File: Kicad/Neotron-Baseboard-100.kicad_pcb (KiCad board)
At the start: 4 copper layers, 243.8 x 170.2 mm, 252 parts, among them J1001 USB Ports External, J1002 USB Ports Internal, J101 Neotron-Expansion-Slot, J102 Neotron-Expansion-Slot, J103 Neotron-Expansion-Slot, J104 Neotron-Expansion-Slot, J1101 RJ45 MagJack, J201 DE15HD, J601 Line Out, J602 AC'97 Audio Header, J603 CD Audio In, J701 SD_Card, J801 Conn_02x05, J802 DB9_Male_MountingHoles, J901 Jack-DC, J902 Conn_01x04, J903 Double-mini-DIN-6, SW901 SW_DIP_x01, SW902 SW_DIP_x01, U1001 AP2501, U1002 MIC2005A-2YM5, U1003 MIC2005A-2YM5, U1004 XR22404CG28, U1005 MIC2005A-2YM5, U1006 MIC2005A-2YM5, U101 Neotron-CPU, U1101 ENC424J600, U1201 MCP7940, U201 THS7316, U202 TPD7S019, U601 TLV320AIC23BPW, U602 STX-4335-5BGP-S1, U801 ST3232CDR, U901 5V DC-DC Module, U902 3v3 LDO, U903 MAX1615, U904 MKE04P24M48SF0, Y1001 12M, Y1101 25M, Y1201 32,768 Hz, Y601 12M

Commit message: Updating to common 0.5.0
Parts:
- removed the J902 at (226.9, 52.6)
- removed the R903 at (223.9, 58.2)
- added C909: 100n, Capacitor_SMD:C_0805_2012Metric_Pad1.15x1.40mm_HandSolder, F.Cu at (241.5, 98.0)
- added JP901: Jumper, Connector_PinHeader_2.54mm:PinHeader_1x02_P2.54mm_Vertical, F.Cu at (239.0, 105.7)
- added JP902: Jumper, Connector_PinHeader_2.54mm:PinHeader_1x02_P2.54mm_Vertical, F.Cu at (246.4, 105.7)
- added JP903: Jumper, Connector_PinHeader_2.54mm:PinHeader_1x02_P2.54mm_Vertical, F.Cu at (243.8, 105.7)
- added Q901: BC548, Package_TO_SOT_THT:TO-92_HandSolder, F.Cu at (246.8, 93.0)
- added R904: 10k, Resistor_SMD:R_0805_2012Metric_Pad1.15x1.40mm_HandSolder, F.Cu at (256.2, 97.8)
- added R909: 10k, Resistor_SMD:R_0805_2012Metric_Pad1.15x1.40mm_HandSolder, F.Cu at (256.2, 107.8)
- added TP902: TestPoint, Connector_PinHeader_2.54mm:PinHeader_1x01_P2.54mm_Vertical, F.Cu at (236.4, 108.3)
- added TP903: TestPoint, Connector_PinHeader_2.54mm:PinHeader_1x01_P2.54mm_Vertical, F.Cu at (241.5, 108.3)
- C901, C902: footprint Capacitor_THT:CP_Radial_D8.0mm_P3.50mm -> Capacitor_THT:CP_Radial_D6.3mm_P2.50mm
- C905: value 47u -> 1u; footprint Capacitor_THT:CP_Radial_D6.3mm_P2.50mm -> Capacitor_SMD:C_0805_2012Metric_Pad1.15x1.40mm_HandSolder
- F901: value 6A PTC -> 32V 2A PTC; footprint Fuse:Fuse_Bourns_MF-RG500 -> Fuse:Fuse_BelFuse_0ZRE0016FF_L9.9mm_W3.8mm
- L901: value 22u -> 22uH 6A; footprint Inductor_THT:L_Axial_L23.4mm_D12.7mm_P7.62mm_Vertical_Vishay_IHA-203 -> Inductor_THT:L_Axial_L26.0mm_D11.0mm_P7.62mm_Vertical_Fastron_77A
- R901: value 100k -> 2k
- R902, R905, R907, R908: value 100k -> 10k
- R906: value 33k -> 10k
- TP901: value Reset -> TestPoint; footprint TestPoint:TestPoint_THTPad_2.0x2.0mm_Drill1.0mm -> Connector_PinHeader_2.54mm:PinHeader_1x01_P2.54mm_Vertical
- U902: value 3v3 LDO -> TLV1117 3.3V 1A; footprint Package_TO_SOT_SMD:TO-252-3_TabPin2 -> Package_TO_SOT_SMD:SOT-223-3_TabPin2
- U904: value MKE04P24M48SF0 -> STM32F030F4Px; footprint Package_SO:SOIC-20W_7.5x12.8mm_P1.27mm -> Package_SO:TSSOP-20_4.4x6.5mm_P0.65mm
- Y1201: footprint Crystal:Crystal_C26-LF_D2.1mm_L6.5mm_Horizontal -> Crystal:Crystal_DS26_D2.0mm_L6.0mm_Horizontal
- moved TP901 291.5 mm to (239.0, 108.3), turned to 180 degrees
- moved SW901 61.6 mm to (255.2, 114.9)
- moved SW902 61.6 mm to (255.2, 110.9)
- moved R902 51.1 mm to (256.2, 93.8), turned to 0 degrees
- moved D901 46.4 mm to (258.0, 119.2)
- moved R907 42.1 mm to (256.2, 103.8)
- moved C908 40.3 mm to (251.5, 98.0), turned to 90 degrees
- moved R903 38.8 mm to (256.2, 95.8), turned to 0 degrees
- moved R905 36.7 mm to (256.2, 99.8)
- moved R908 35.7 mm to (256.2, 105.8), turned to 180 degrees
- moved R906 33.8 mm to (256.2, 101.8), turned to 0 degrees
- moved U904 33.8 mm to (246.5, 100.0)
- moved U902 29.0 mm to (257.8, 74.3), turned to 90 degrees
- moved R901 27.5 mm to (256.2, 91.8), turned to 180 degrees
- moved C905 25.2 mm to (256.3, 80.0)
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- renumbered J903 to J902, R904 to R903
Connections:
- C907 pad 1: +5VP -> +3.3VP
- C908 pad 1: +5VP -> +3.3VP
- R901 pad 1: /Power Supply/DC_ON -> Net-(Q901-Pad2)
- R901 pad 2: GND -> /Power Supply/DC_ON
- R902 pad 1: +5VP -> /Power Supply/DC_ON
- R902 pad 2: /Power Supply/SWDCLK -> GND
- R903 pad 1: /Power Supply/STATUS_LED -> /Power Supply/~STATUS_LED
- R905 pad 2: /Power Supply/MON_5V -> Net-(R905-Pad2)
- R907 pad 1: /Power Supply/MON_5V -> Net-(R905-Pad2)
- R907 pad 2: GND -> /Power Supply/MON_5V
- RN901 pad 4: /Power Supply/PS2_DAT1 -> /Power Supply/PS2_CLK1
- RN901 pad 5: /Power Supply/PS2_CLK1 -> /Power Supply/PS2_DAT1
- SW901 pad 2: /Power Supply/~RESET_SW -> /Power Supply/~BUTTON_RST
- SW902 pad 2: /Power Supply/~POWER_SW -> /Power Supply/~BUTTON_PWR
- TP901 pad 1: Net-(TP901-Pad1) -> /Power Supply/USART1_TX
- U101 pad 4.3: /SD Card/DAT2 -> /SD Card/DAT1
- U101 pad 4.4: /SD Card/DAT3 -> /SD Card/DAT0
- U101 pad 4.5: /SD Card/CMD -> /SD Card/CLK
- U101 pad 4.6: /SD Card/CLK -> /SD Card/CMD
- U101 pad 4.7: /SD Card/DAT0 -> /SD Card/DAT3
- U101 pad 4.8: /SD Card/DAT1 -> /SD Card/DAT2
- U901 pad 1: /Power Supply/DC_ON -> /Power Supply/~PSU_EN
- U903 pad 3: +5VP -> +3.3VP
- U903 pad 4: +5VP -> GND
- U904 pad 1: Net-(TP901-Pad1) -> /Power Supply/BOOT0
- U904 pad 10: /Power Supply/PS2_CLK1 -> /Power Supply/DC_ON
- U904 pad 11: /Power Supply/PS2_DAT0 -> /~RESET
- U904 pad 12: /Power Supply/PS2_CLK0 -> /Power Supply/~BUTTON_RST
- U904 pad 13: /Power Supply/~RESET_SW -> /Power Supply/~BUTTON_PWR
- U904 pad 15: /Power Supply/UART0_TX -> GND
- U904 pad 16: /Power Supply/MON_3V3 -> +3.3VP
- U904 pad 17: /I2C_SCL -> /Power Supply/SCL_U1TX
- U904 pad 18: /I2C_SDA -> /Power Supply/SDA_U1RX
- U904 pad 19: /Power Supply/MON_5V -> /Power Supply/PS2_DAT1
- U904 pad 2: /Power Supply/SWDIO -> /Power Supply/PS2_DAT0
- U904 pad 20: /Power Supply/SWDCLK -> /Power Supply/PS2_CLK1
- U904 pad 3: +5VP -> /Power Supply/PS2_CLK0
- U904 pad 4: GND -> /Power Supply/~BMC_RST
- U904 pad 5: /Power Supply/STATUS_LED -> +3.3VP
- U904 pad 6: /Power Supply/DC_ON -> /Power Supply/MON_3V3
- U904 pad 7: /~RESET -> /Power Supply/MON_5V
- U904 pad 8: /Power Supply/~POWER_SW -> /Power Supply/USART1_TX
- U904 pad 9: /Power Supply/PS2_DAT1 -> /Power Supply/~STATUS_LED
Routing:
- net +5V: track 716.5 -> 130.8 mm, vias 9 -> 2
- net /~CS0: track 356.5 -> 0.00 mm, vias 1 -> 0
- net /~IRQ0: track 353.0 -> 0.00 mm, vias 1 -> 0
- net /I2C_SCL: track 337.1 -> 0.00 mm, vias 2 -> 0
- net /I2C_SDA: track 332.6 -> 0.00 mm, vias 2 -> 0
- net /~CS1: track 327.9 -> 0.00 mm, vias 1 -> 0
- net /~IRQ1: track 325.6 -> 0.00 mm, vias 1 -> 0
- net /~IRQ2: track 282.7 -> 0.00 mm
- net /~CS2: track 278.2 -> 0.00 mm
- net /~CS3: track 259.5 -> 0.00 mm
- net /~IRQ3: track 259.4 -> 0.00 mm
- net /~RESET: track 248.8 -> 0.00 mm, vias 2 -> 0
- net /SPI_CLK: track 215.1 -> 0.00 mm, vias 1 -> 0
- net /SPI_COPI: track 214.9 -> 0.00 mm, vias 1 -> 0
- net /SPI_CIPO: track 213.1 -> 0.00 mm, vias 1 -> 0
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
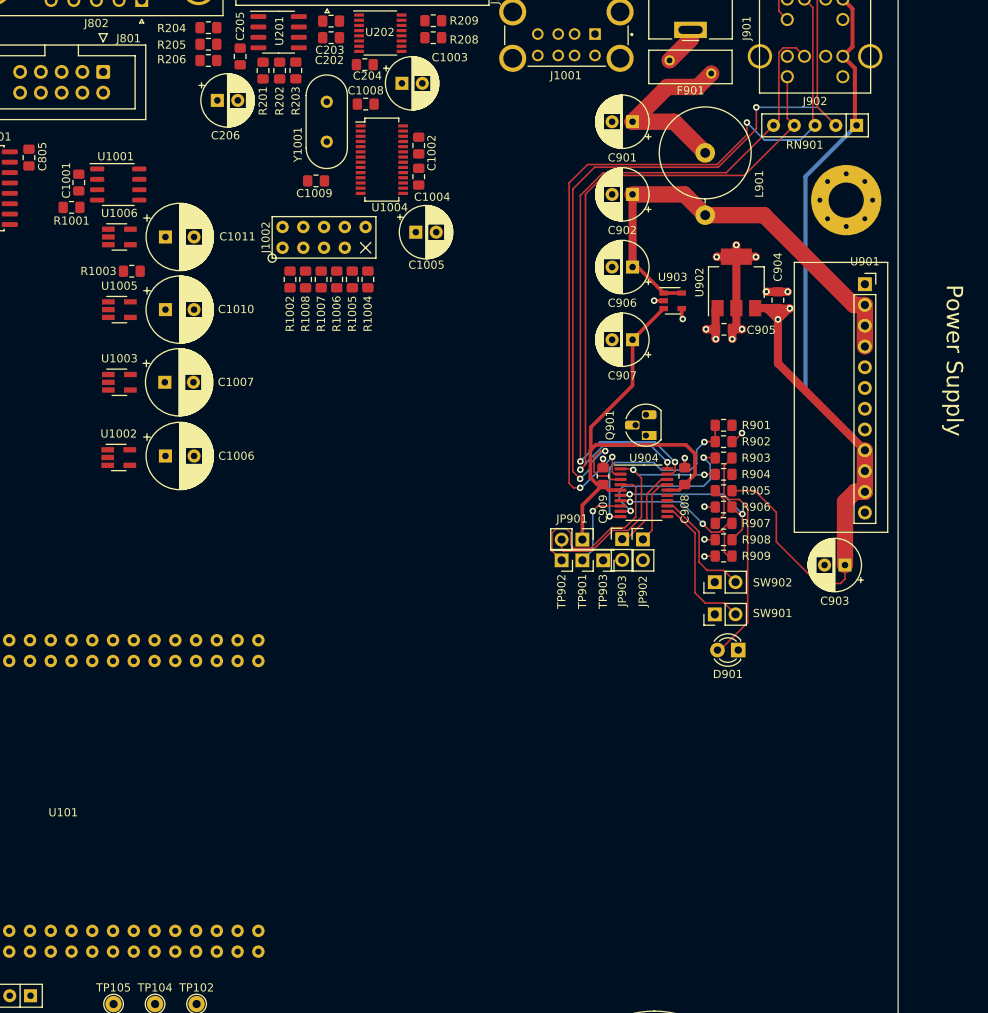
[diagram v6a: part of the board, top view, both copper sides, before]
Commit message: Updated to v0.6.0
Started re-laying out PSU
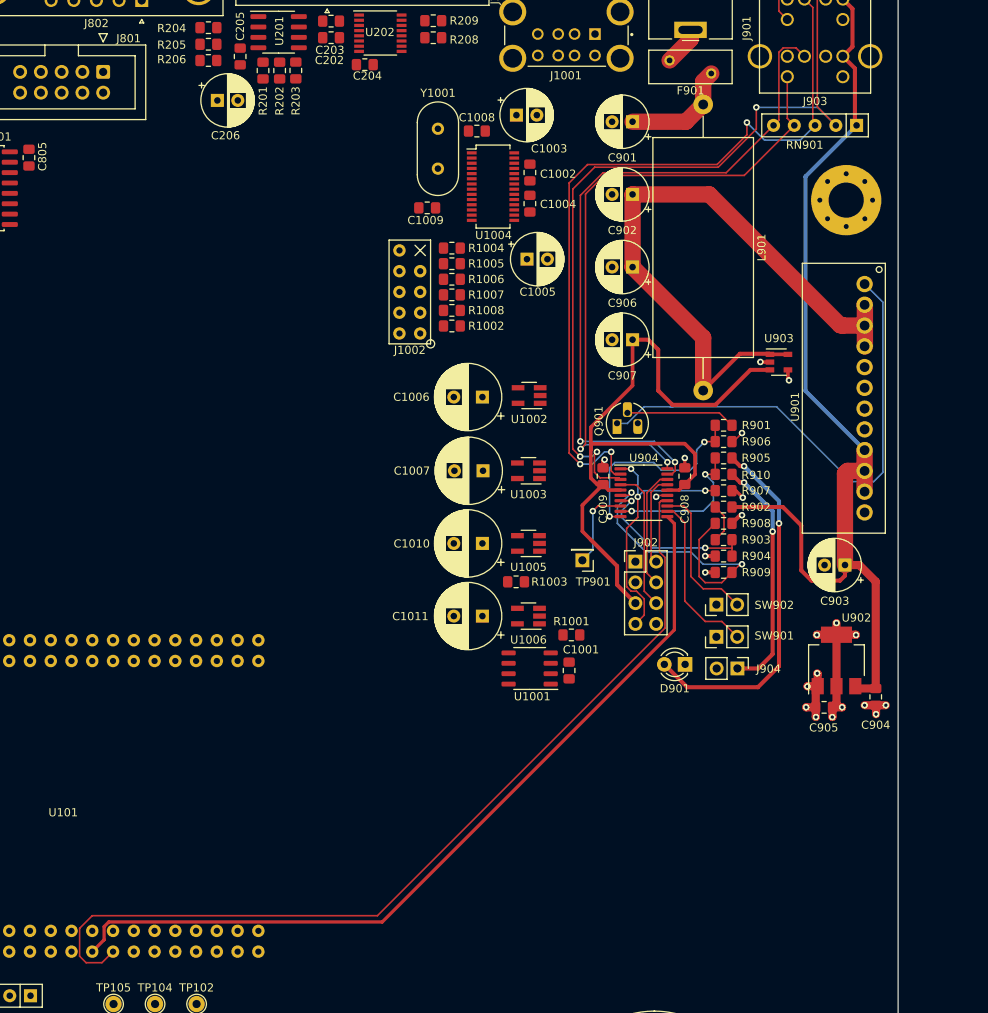
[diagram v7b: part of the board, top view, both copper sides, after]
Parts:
- removed JP901, JP902, JP903: Jumper, Connector_PinHeader_2.54mm:PinHeader_1x02_P2.54mm_Vertical
- removed the R909 at (256.2, 107.8)
- removed TP902, TP903: TestPoint, Connector_PinHeader_2.54mm:PinHeader_1x01_P2.54mm_Vertical
- added J902: Conn_02x04_Odd_Even, Connector_PinHeader_2.54mm:PinHeader_2x04_P2.54mm_Vertical, F.Cu at (245.5, 108.4)
- added J904: Header, Connector_PinHeader_2.54mm:PinHeader_1x02_P2.54mm_Vertical, F.Cu at (257.9, 121.5)
- added R904: 10k, Resistor_SMD:R_0805_2012Metric_Pad1.15x1.40mm_HandSolder, F.Cu at (256.2, 107.8)
- added R910: 1k, Resistor_SMD:R_0805_2012Metric_Pad1.15x1.40mm_HandSolder, F.Cu at (256.2, 97.8)
- L901: footprint Inductor_THT:L_Axial_L26.0mm_D11.0mm_P7.62mm_Vertical_Fastron_77A -> Inductor_THT:L_Axial_L26.7mm_D12.1mm_P35.00mm_Horizontal_Vishay_IHA-103
- U901: footprint Connector_PinSocket_2.54mm:PinSocket_1x12_P2.54mm_Vertical -> Neotron-Common-Hardware:K78xx-3AR3
- moved C1001 84.6 mm to (237.3, 121.8), turned to 270 degrees
- moved R1001 80.5 mm to (237.6, 117.4), turned to 180 degrees
- moved U1001 77.7 mm to (232.5, 121.5), turned to 180 degrees
- moved U1006 68.2 mm to (232.4, 115.1), turned to 180 degrees
- moved C1011 60.5 mm to (226.7, 115.1), turned to 180 degrees
- moved R1003 60.5 mm to (230.9, 110.9), turned to 0 degrees
- moved U1005 57.6 mm to (232.4, 106.2), turned to 180 degrees
- moved U1003 51.2 mm to (232.4, 97.3), turned to 180 degrees
- moved U1002 50.8 mm to (232.5, 88.1), turned to 180 degrees
- moved C904 50.0 mm to (274.9, 125.0), turned to 270 degrees
- moved C1010 48.2 mm to (226.7, 106.2), turned to 180 degrees
- moved C905 47.8 mm to (268.5, 126.3)
- moved U902 47.8 mm to (270.1, 120.5)
- moved C1007 40.4 mm to (226.8, 97.3), turned to 180 degrees
- moved C1006 39.4 mm to (226.7, 88.3), turned to 180 degrees
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- renumbered J902 to J903, R905 to R902, R907 to R903, R903 to R905, R902 to R906, R904 to R907, R906 to R908, R908 to R909
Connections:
- U901 pad 3: Net-(C902-Pad1) -> GND
- U901 pad 4: Net-(C902-Pad1) -> +5V
- U901 pad 5: GND -> (no net)
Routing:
- net /~IRQ7: track 0.59 -> 112.5 mm
- net /~RESET: track 0.00 -> 102.7 mm
- net /Power Supply/~PSU_EN: track 0.00 -> 61.6 mm
- net +3.3VP: track 56.6 -> 87.0 mm
- net Net-(J904-Pad1): track 0.00 -> 29.4 mm, vias 0 -> 2
- net Net-(C902-Pad1): track 55.3 -> 80.6 mm
- net Net-(D901-Pad2): track 27.6 -> 44.4 mm, vias 0 -> 2
- net /Power Supply/MON_3V3: track 21.3 -> 37.1 mm
- net Net-(Q901-Pad2): track 0.00 -> 13.2 mm
- net Net-(C901-Pad1): track 22.5 -> 13.7 mm
- net GND: track 16.8 -> 24.9 mm, vias 11 -> 16
- net +5V: track 130.8 -> 123.9 mm, vias 2 -> 0
- net /Power Supply/PS2_CLK0: track 111.7 -> 105.5 mm
- net /Power Supply/~BMC_RST: track 23.3 -> 17.4 mm
- net /Power Supply/SDA_U1RX: track 10.3 -> 14.6 mm
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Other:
- board text removed: "Power Supply"
